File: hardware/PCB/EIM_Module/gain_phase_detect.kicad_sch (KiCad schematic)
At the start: 1 part, among them U9 AD8302ARUZ

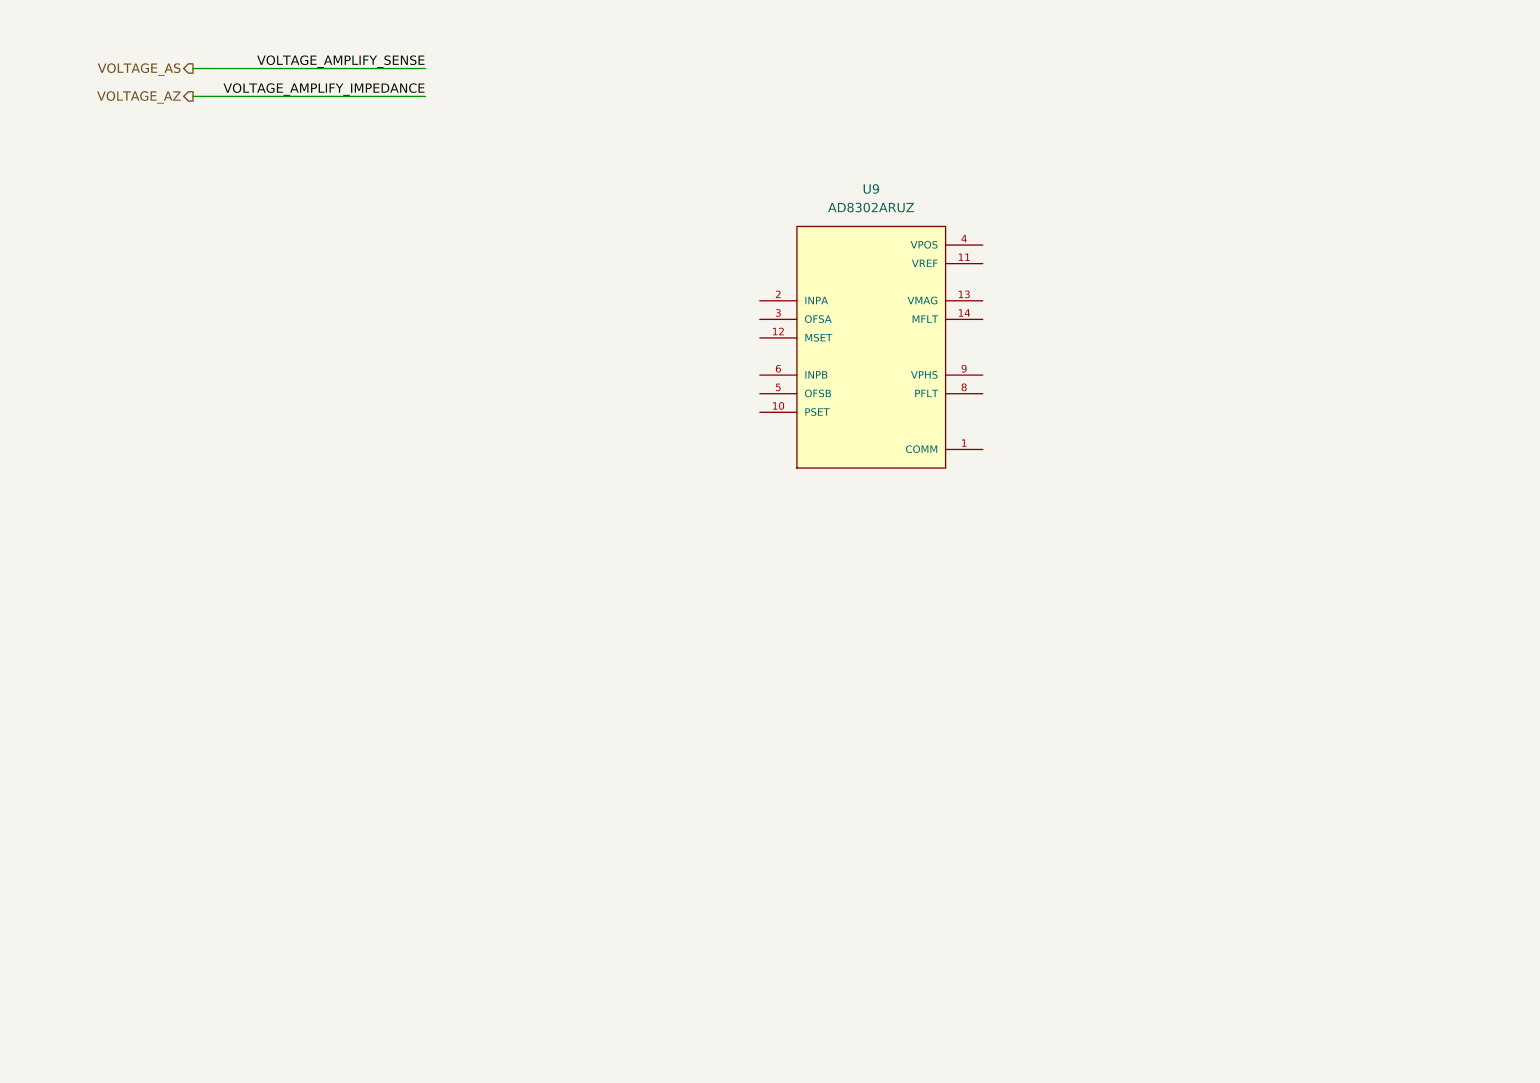
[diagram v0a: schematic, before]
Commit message: MAMS-33 Updated simulation final and update schematic and PCB
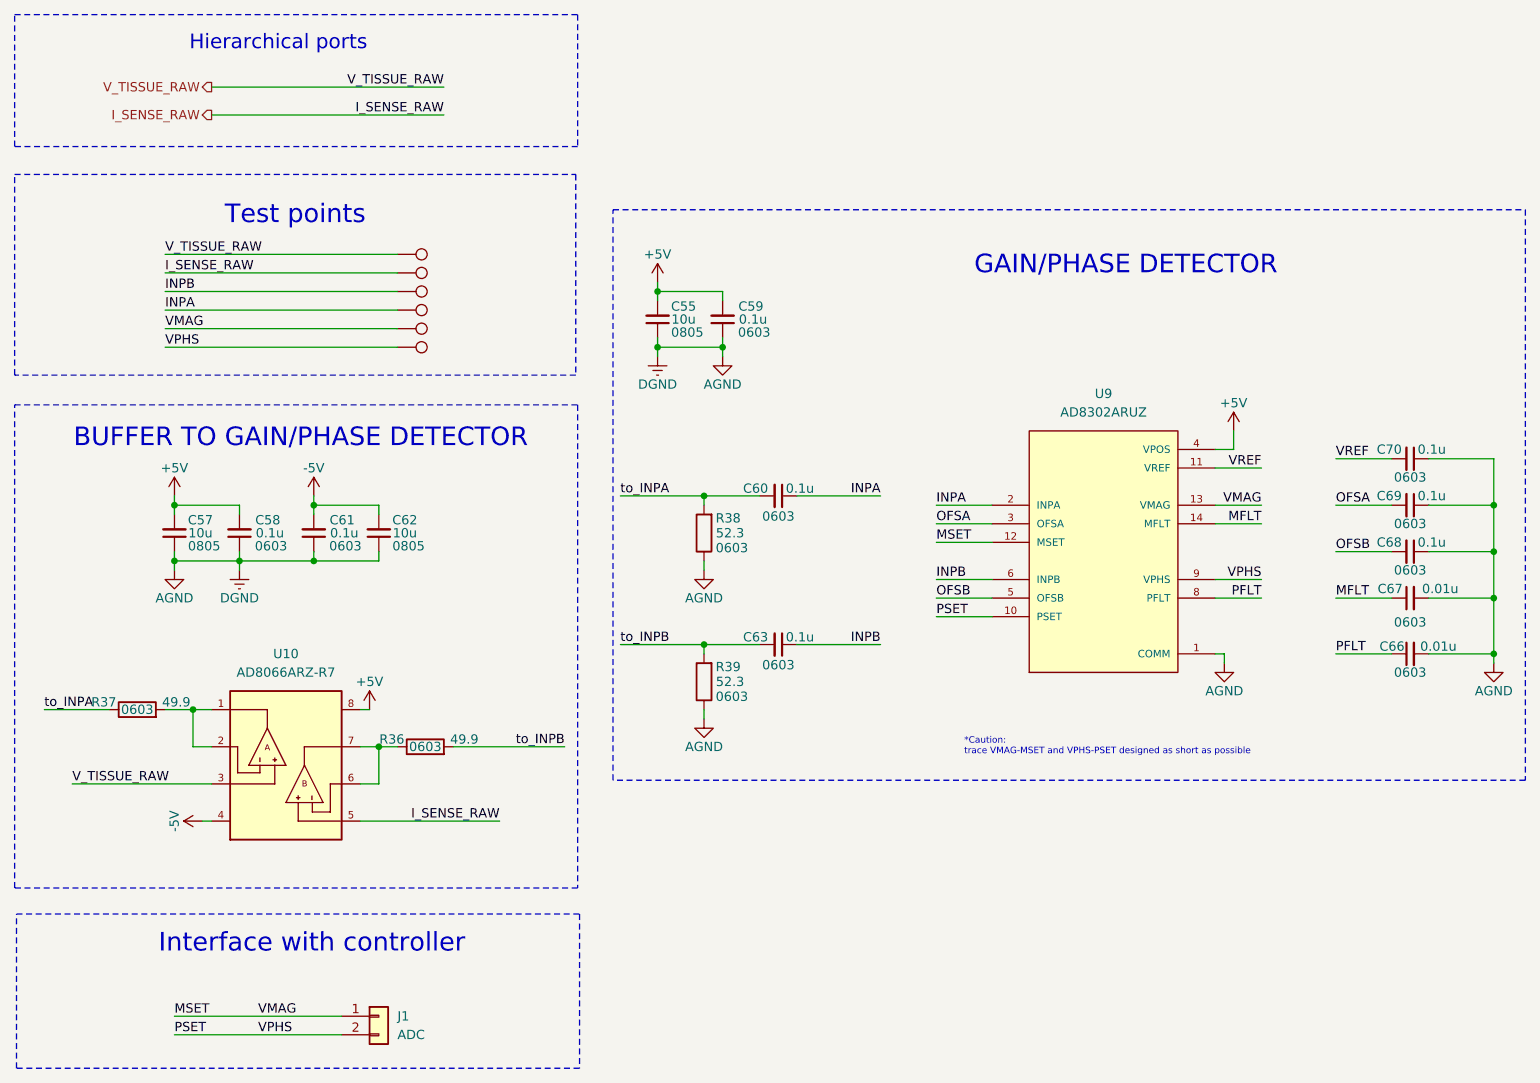
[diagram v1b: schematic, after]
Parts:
- added C55, C57, C62: 10u, Capacitor_SMD:C_0805_2012Metric, symbol Device:C_Small
- added C58, C59, C60, C61, C63, C68, C69, C70: 0.1u, Capacitor_SMD:C_0603_1608Metric, symbol Device:C_Small
- added C66, C67: 0.01u, Capacitor_SMD:C_0603_1608Metric, symbol Device:C_Small
- added J1: ADC, Connector_JST:JST_PH_S2B-PH-K_1x02_P2.00mm_Horizontal, symbol Connector_Generic:Conn_01x02
- added R36, R37: 49.9, Resistor_SMD:R_0603_1608Metric, symbol Device:R
- added R38, R39: 52.3, Resistor_SMD:R_0603_1608Metric, symbol Device:R
- added TP21: VOUT_FILTERED, TestPoint:TestPoint_Pad_D1.0mm, symbol Connector:TestPoint
- added TP26: VOUT_BUFFER, TestPoint:TestPoint_Pad_D1.0mm, symbol Connector:TestPoint
- added TP27: VIN_DiffToSingle, TestPoint:TestPoint_Pad_D1.0mm, symbol Connector:TestPoint
- added TP28, TP30, TP31: TP_GND, TestPoint:TestPoint_Pad_D1.0mm, symbol Connector:TestPoint
- added U10: AD8066ARZ-R7, AD8066ARZ:SOIC127P600X175-8N, symbol AD8066:AD8066ARZ-R7
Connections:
- net PSET: now reaches U9.10 (PSET)
- net PSET: now also U9.9 (VPHS), J1.2 (Pin_2), TP31.1
- net VREF: now reaches U9.11 (VREF)
- net VREF: now also C70.2
- net MSET: now reaches U9.12 (MSET)
- net MSET: now also U9.13 (VMAG), J1.1 (Pin_1), TP30.1
- net MFLT: now reaches U9.14 (MFLT)
- net MFLT: now also C67.1
- net INPA: now reaches U9.2 (INPA)
- net INPA: now also C60.1, TP21.1
- net OFSA: now reaches U9.3 (OFSA)
- net OFSA: now also C69.2
- net +5V: now reaches U9.4 (VPOS)
- net +5V: now also C55.2, C57.2, C58.2, C59.2, U10.8
- net OFSB: now reaches U9.5 (OFSB)
- net OFSB: now also C68.2
- net INPB: now reaches U9.6 (INPB)
- net INPB: now also C63.1, TP28.1
- net PFLT: now reaches U9.8 (PFLT)
- net PFLT: now also C66.1
- net COMM renamed AGND
- net AGND: now also C55.1, C57.1, C58.1, C59.1, C61.1, C62.1, C66.2, C67.2, C68.1, C69.1, C70.1, R38.1, R39.1
- new net: R36.1, U10.6, U10.7
- new net: R37.2, U10.1, U10.2
- new net -5V: C61.2, C62.2, U10.4
- new net I_SENSE_RAW: TP27.1, U10.5
- new net V_TISSUE_RAW: TP26.1, U10.3
- new net to_INPA: C60.2, R37.1, R38.2
- new net to_INPB: C63.2, R36.2, R39.2
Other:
- note added: "*Caution: trace VMAG-MSET and VPHS-PSET designed as short as possible"
- note added: "BUFFER TO GAIN/PHASE DETECTOR"
- note added: "GAIN/PHASE DETECTOR"
- note added: "Hierarchical ports"
- note added: "Interface with controller"
- note added: "Test points"
- moved on the sheet: U9

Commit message: MAMS-38 updated PCB layout for EIM with version using connector
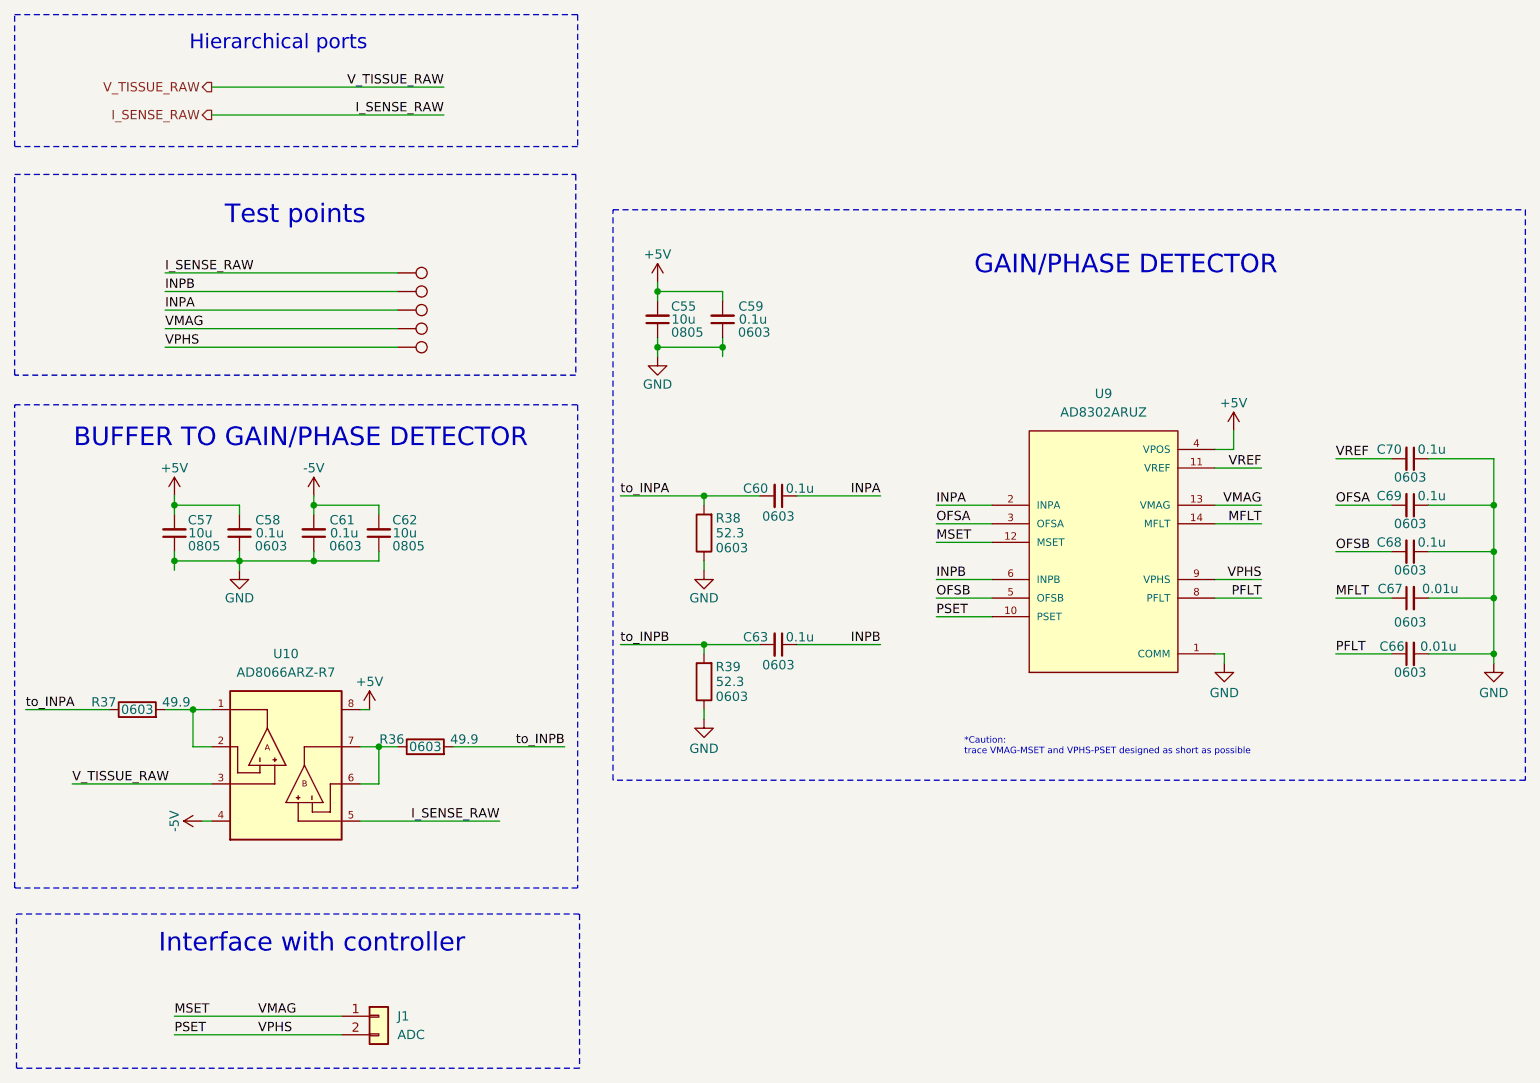
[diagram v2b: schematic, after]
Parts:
- removed TP26: VOUT_BUFFER, TestPoint:TestPoint_Pad_D1.0mm, symbol Connector:TestPoint
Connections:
- net AGND renamed COMM

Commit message: MAMS-40 Updated PCB upto LPF
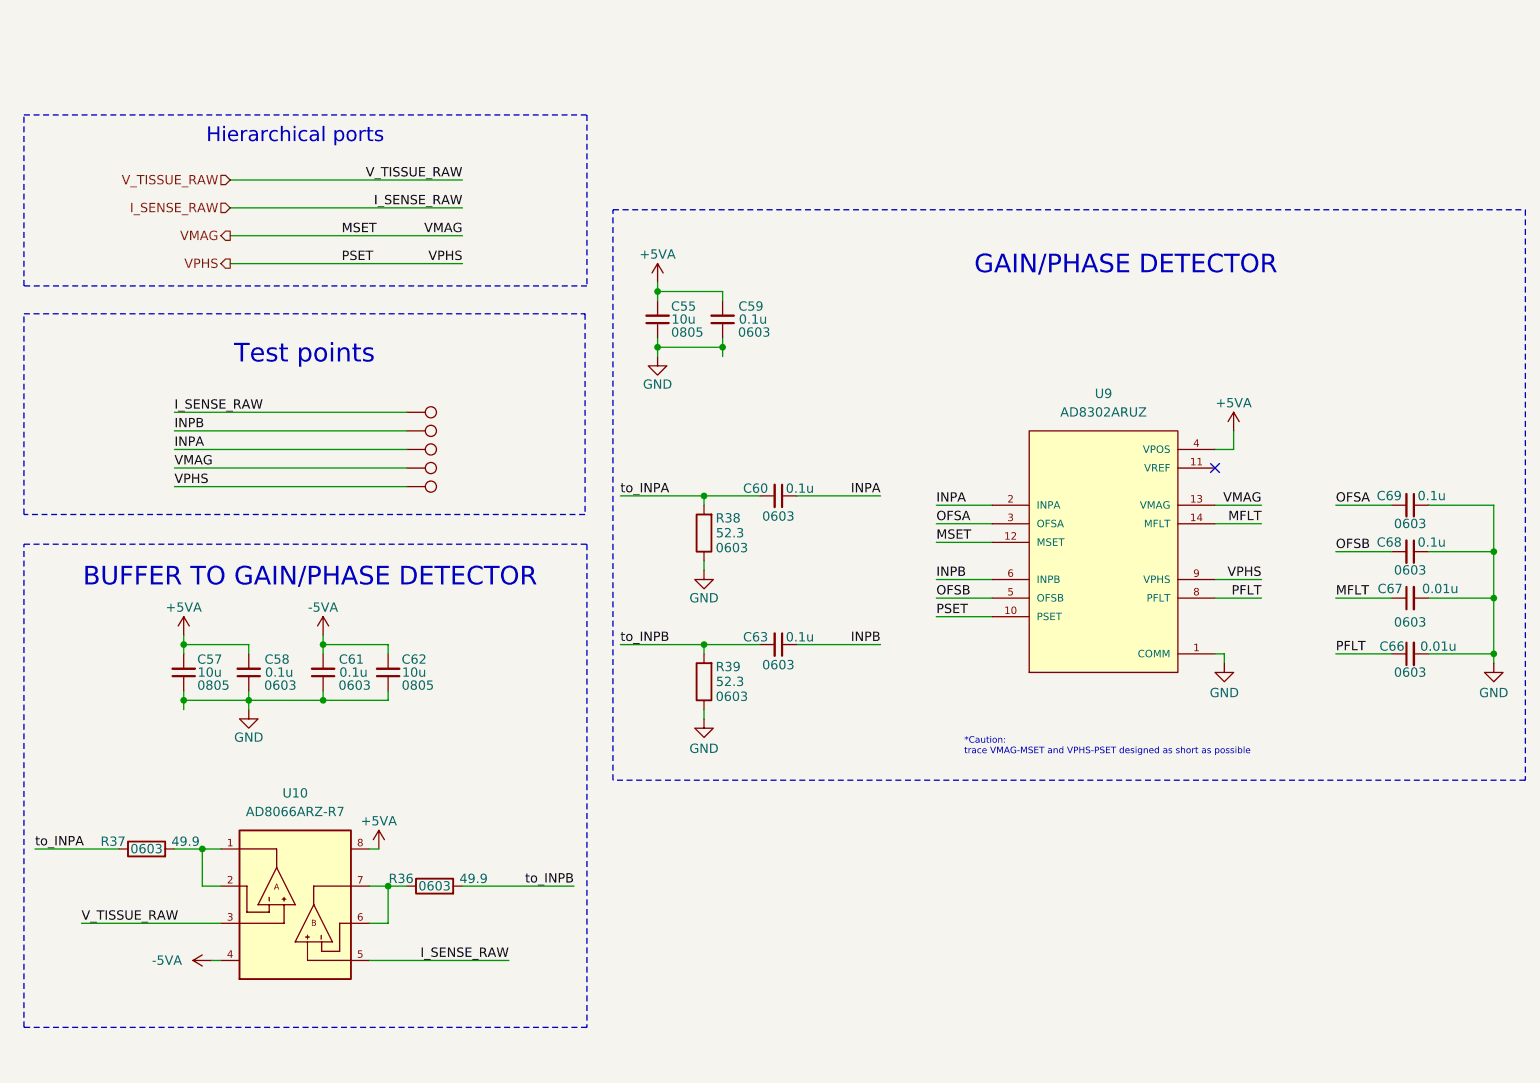
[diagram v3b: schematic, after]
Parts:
- removed C70: 0.1u, Capacitor_SMD:C_0603_1608Metric, symbol Device:C_Small
- removed J1: ADC, Connector_JST:JST_PH_S2B-PH-K_1x02_P2.00mm_Horizontal, symbol Connector_Generic:Conn_01x02
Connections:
- net +5V renamed +5VA
- net -5V renamed -5VA
- net MSET renamed VMAG
- net PSET renamed VPHS
- net VREF: no longer names the net of U9.11 (VREF)
- no-connect marks 0 -> 1
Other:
- note removed: "Interface with controller"
- moved on the sheet: C57, C58, C61, C62, R36, R37, U10
